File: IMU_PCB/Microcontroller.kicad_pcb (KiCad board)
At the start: 2 copper layers, 103.7 x 64.2 mm, 29 parts, among them J1 Conn_01x02, J4 Conn_01x02_Pin, U1 TPS54560BQDDARQ1, U10 Thermal Resistor, U2 ESP32-DEVKIT-C, U6 TJA1050T/CM,118, U7 Adafruit ICM-20948, U8 SDIO Card Breakout Board, U9 AM2302

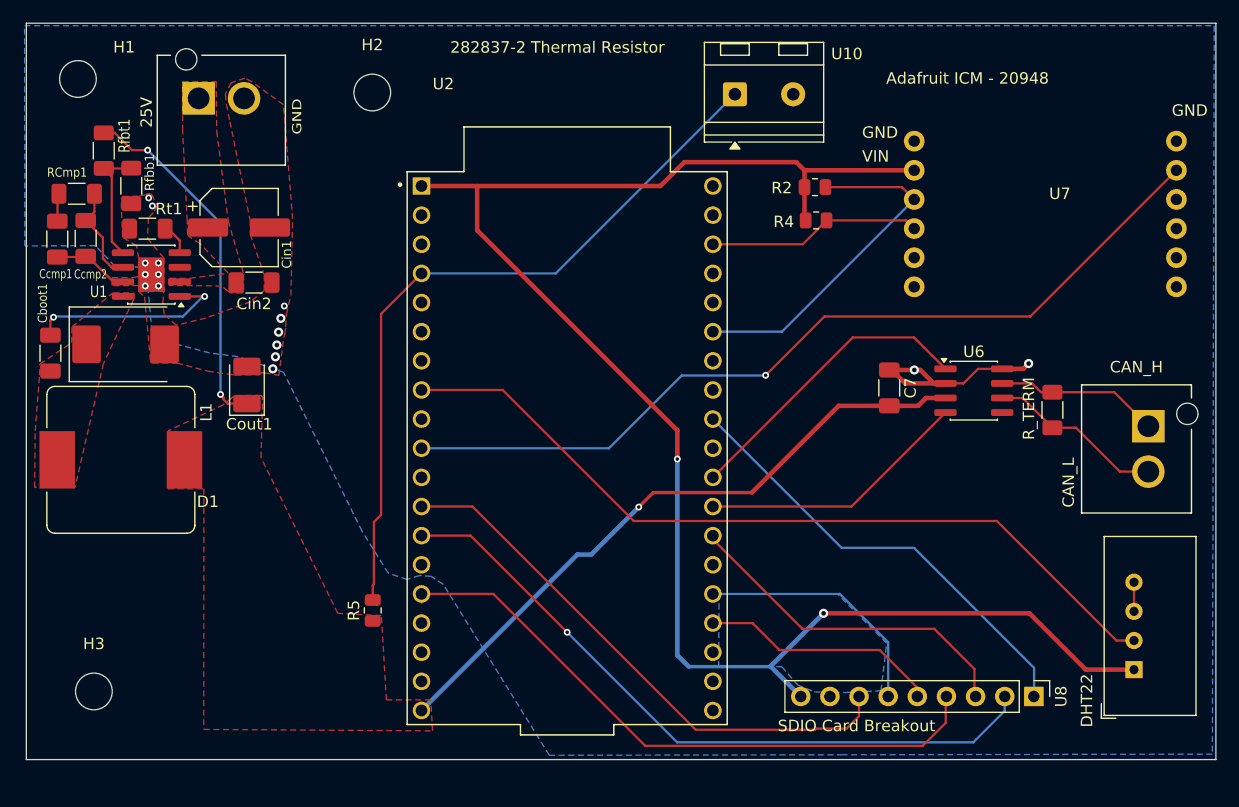
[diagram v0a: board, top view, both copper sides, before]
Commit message: small updates to buck, fixed vias, and remove connection to input connector ground pad
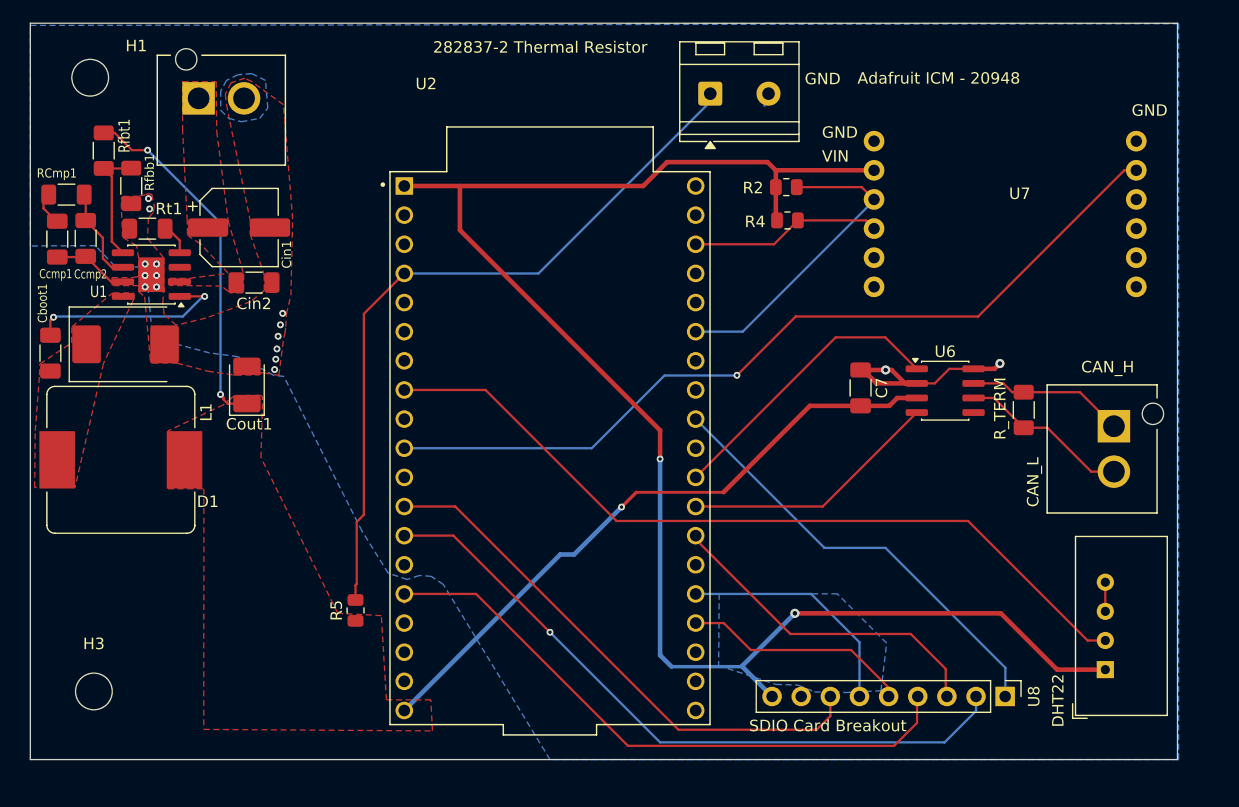
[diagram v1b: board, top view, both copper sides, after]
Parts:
- removed H2: MountingHole, MountingHole:MountingHole_3.2mm_M3
- moved U7 3.50 mm to (186.8, 62.7)
- moved J4 3.00 mm to (193.9, 81.9)
- moved C7 2.50 mm to (172.9, 76.6)
- moved R2 2.50 mm to (166.4, 59.1)
- moved R4 2.50 mm to (166.5, 62.0)
- moved R8 2.50 mm to (187.1, 78.5)
- moved U6 2.50 mm to (180.2, 76.8)
- moved U8 2.50 mm to (185.5, 103.5)
- moved U9 2.50 mm to (194.2, 101.2)
- moved U10 2.15 mm to (159.8, 51.0)
- moved R5 1.50 mm to (128.8, 96.0)
- moved U2 1.50 mm to (145.8, 81.8)
- moved H1 1.08 mm to (105.7, 49.6)
- moved RCmp1 0.89 mm to (103.7, 59.8)
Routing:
- net Net-(U2-3V3): track 149.4 -> 146.4 mm
- net Net-(U2-IO21): track 30.5 -> 27.6 mm
- net Net-(U2-IO22): track 18.7 -> 16.7 mm
- net Net-(U2-IO26): track 75.9 -> 73.9 mm
- net Net-(U2-IO4): track 30.2 -> 29.2 mm
- net Net-(U2-IO33): track 71.2 -> 70.2 mm
- net Net-(U2-IO2): track 21.7 -> 20.7 mm
- net Net-(U2-IO18): track 39.4 -> 38.4 mm
- net Net-(U2-IO17): track 26.5 -> 25.5 mm
- net Net-(U2-IO16): track 23.7 -> 22.7 mm
- net Net-(U2-IO15): track 20.9 -> 19.9 mm
- net Net-(U2-IO13): track 55.1 -> 54.1 mm
- net Net-(U2-IO12): track 61.0 -> 60.0 mm
- net Net-(U2-IO14): track 48.7 -> 47.7 mm
- net /BUCK_5V: track 87.8 -> 86.8 mm
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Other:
- board size 103.7 x 64.2 mm -> 100 x 64.2 mm
- board text removed: "25V"

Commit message: PDB_Schematic mostly updated
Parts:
- removed R2, R4: 10k, Resistor_SMD:R_0805_2012Metric
- added H2: MountingHole, MountingHole:MountingHole_3.2mm_M3, F.Cu at (196.2, 56.2)
- added H4: MountingHole, MountingHole:MountingHole_3.2mm_M3, F.Cu at (195.8, 106.9)
- U10: footprint TerminalBlock_RND:TerminalBlock_RND_205-00232_1x02_P5.08mm_Horizontal -> PROVE-footprints:TE_1877285-2
- U7: value Adafruit ICM-20948 -> SparkFun: ISM330DHCX, MMC5983MA; footprint PROVE-footprints:Adafruit_ICM20948_2x6_Module -> PROVE-footprints:SparkFun 9DoF IMU Breakout - ISM330DHCX, MMC5983MA (Qwiic); moved to B.Cu
- U8: footprint Connector_PinHeader_2.54mm:PinHeader_1x09_P2.54mm_Vertical -> PROVE-footprints:Adafruit SDIO card breakout
- moved U10 47.3 mm to (194.2, 83.4), turned to -90 degrees
- moved R5 44.8 mm to (172.8, 104.8)
- moved U6 29.8 mm to (184.0, 106.4)
- moved C7 29.3 mm to (178.6, 105.3)
- moved U9 28.7 mm to (192.9, 72.5)
- moved R8 26.3 mm to (190.4, 104.6)
- moved U7 15.8 mm to (188.0, 78.4), turned to 90 degrees
- moved J4 14.1 mm to (194.1, 96.0)
- moved Cin1 7.00 mm to (118.7, 69.6)
- moved Cboot1 7.00 mm to (102.2, 80.6)
- moved Cin2 7.00 mm to (120.0, 74.4)
- moved Cout1 7.00 mm to (119.4, 83.3)
- moved D1 7.00 mm to (108.8, 79.8)
- moved J1 7.00 mm to (117.2, 59.4)
- moved L1 7.00 mm to (108.4, 89.9)
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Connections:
- U2 pad 10: Net-(U2-IO26) -> unconnected-(U2-IO26-Pad10)
- U2 pad 31: unconnected-(U2-IO19-Pad31) -> Net-(U2-IO19)
- U2 pad 37: unconnected-(U2-IO23-Pad37) -> Net-(U2-IO23)
- U6 pad 1: Net-(U2-IO17) -> Net-(U2-IO16)
- U6 pad 4: Net-(U2-IO16) -> Net-(U2-IO17)
- U7 pad 1: GND -> Net-(U2-IO19)
- U7 pad 10: unconnected-(U7-Pin_10-Pad10) -> Net-(U2-IO21)
- U7 pad 11: Net-(U2-IO26) -> Net-(U2-3V3)
- U7 pad 2: Net-(U2-3V3) -> unconnected-(U7-Pin_2-Pad2)
- U7 pad 3: Net-(U2-IO21) -> Net-(U2-IO23)
- U7 pad 4: Net-(U2-IO22) -> unconnected-(U7-Pin_4-Pad4)
- U7 pad 9: unconnected-(U7-Pin_9-Pad9) -> Net-(U2-IO22)
- U8 pad 1: Net-(U2-IO18) -> Net-(U2-3V3)
- U8 pad 2: Net-(U2-IO12) -> GND
- U8 pad 3: Net-(U2-IO4) -> Net-(U2-IO14)
- U8 pad 4: Net-(U2-IO13) -> Net-(U2-IO2)
- U8 pad 6: Net-(U2-IO2) -> Net-(U2-IO13)
- U8 pad 7: Net-(U2-IO14) -> Net-(U2-IO4)
- U8 pad 8: GND -> Net-(U2-IO12)
- U8 pad 9: Net-(U2-3V3) -> Net-(U2-IO18)
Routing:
- net Net-(U2-IO26): track 73.9 -> 0.00 mm, vias 1 -> 0
- net Net-(U10-Pin_1): track 64.0 -> 126.8 mm, vias 0 -> 1
- net /BUCK_5V: track 86.8 -> 46.0 mm, vias 3 -> 6
- net Net-(U2-IO23): track 0.00 -> 35.7 mm
- net Net-(U2-3V3): track 146.4 -> 113.7 mm, vias 2 -> 0
- net Net-(U2-IO19): track 0.00 -> 31.2 mm
- net Net-(U2-IO18): track 38.4 -> 7.73 mm
- net Net-(U2-IO14): track 47.7 -> 76.5 mm, vias 0 -> 1
- net Net-(U2-IO16): track 22.7 -> 50.5 mm
- net Net-(U2-IO17): track 25.5 -> 52.5 mm
- net Net-(U2-IO21): track 27.6 -> 8.24 mm
- net Net-(U2-IO13): track 54.1 -> 67.2 mm
- net Net-(U2-IO4): track 29.2 -> 16.6 mm
- net Net-(U2-IO22): track 16.7 -> 6.16 mm
- net Net-(U2-IO15): track 19.9 -> 29.8 mm, vias 0 -> 1
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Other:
- board size 100 x 64.2 mm -> 100 x 59.2 mm
- board text added: "M3"
- board text removed: "282837-2 Thermal Resistor"

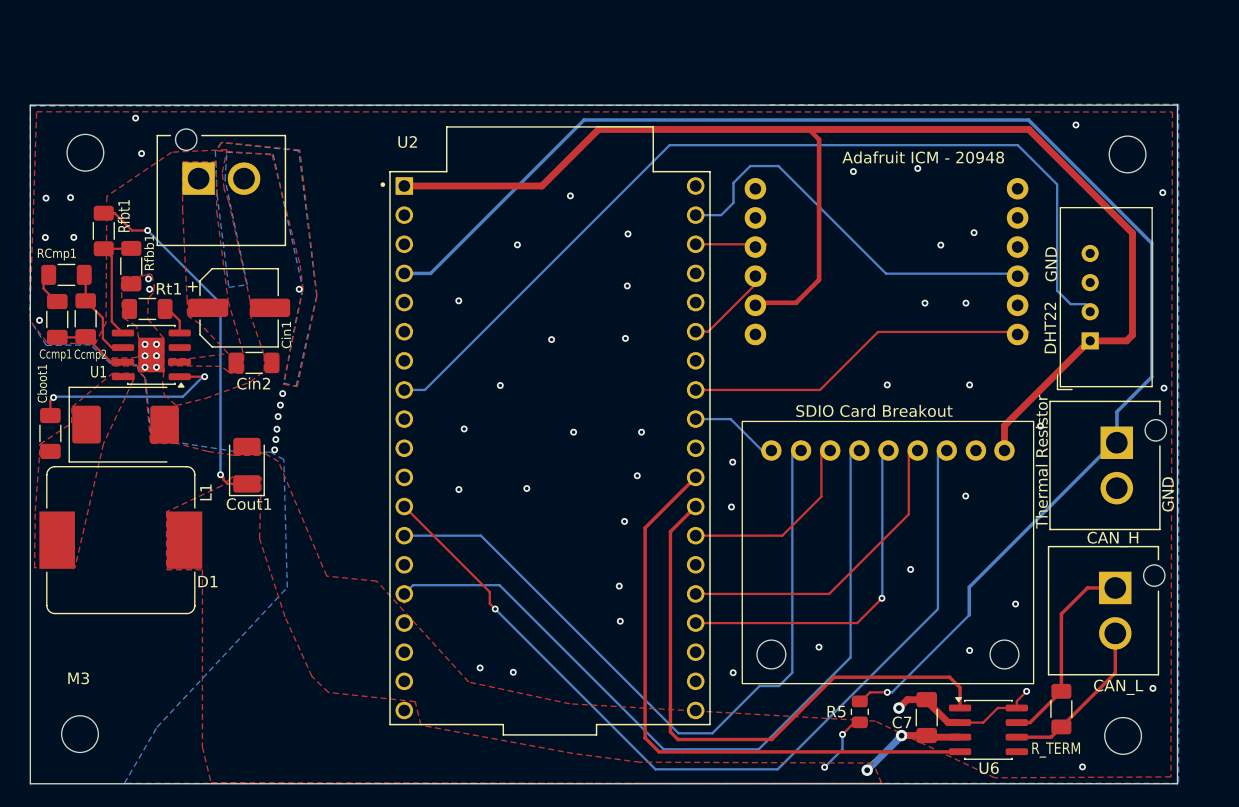
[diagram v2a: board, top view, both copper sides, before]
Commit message: sry forgot to push, waiting on PCB shipping atm. Notes: split power distribution into two boards, one for the main 25V distribution, and another for 12V stuff. Also updated CAN transciever. the previous one was a 5V logic one (same logic as its power), and would have fried our ESPs data pins
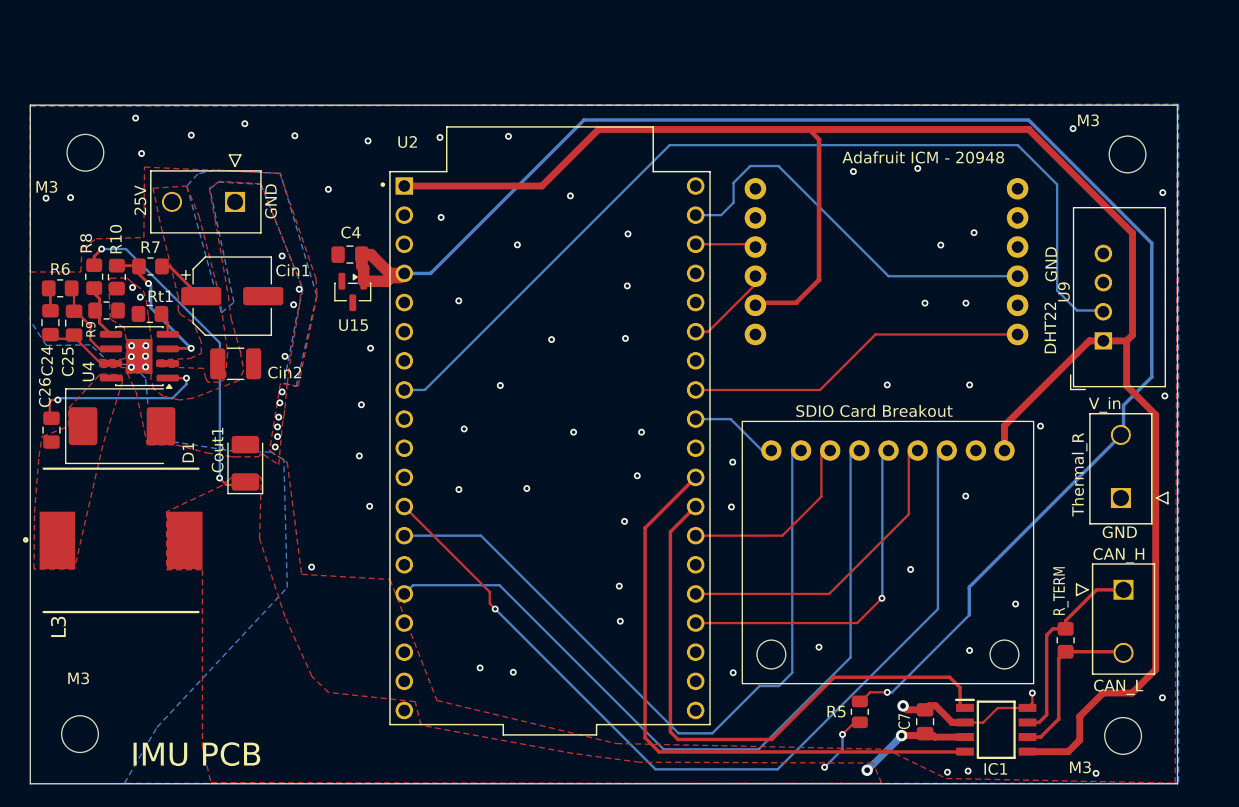
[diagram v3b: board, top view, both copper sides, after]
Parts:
- removed Cboot1: 100nF, Capacitor_SMD:C_1206_3216Metric_Pad1.33x1.80mm_HandSolder
- removed Ccmp1: 10nF, Capacitor_SMD:C_1206_3216Metric_Pad1.33x1.80mm_HandSolder
- removed Ccmp2: 10pF, Capacitor_SMD:C_1206_3216Metric_Pad1.33x1.80mm_HandSolder
- removed J1: Conn_01x02, PROVE-footprints:TE_1877285-2
- removed J4: Conn_01x02_Pin, PROVE-footprints:TE_1877285-2
- removed L1: 22uH, Inductor_SMD:L_Bourns_SRP1245A
- removed RCmp1: 18.2kOhm, Resistor_SMD:R_1206_3216Metric_Pad1.30x1.75mm_HandSolder
- removed Rfbb1: 11.8kOhm, Resistor_SMD:R_1206_3216Metric_Pad1.30x1.75mm_HandSolder
- removed Rfbt1: 64.9kOhm, Resistor_SMD:R_1206_3216Metric_Pad1.30x1.75mm_HandSolder
- removed U1: TPS54560BQDDARQ1, Package_SO:SOIC-8-1EP_3.9x4.9mm_P1.27mm_EP2.29x3mm
- removed U10: Thermal Resistor, PROVE-footprints:TE_1877285-2
- removed U6: TJA1050T/CM,118, Package_SO:SOIC-8_3.9x4.9mm_P1.27mm
- added C24: 10nF, Capacitor_SMD:C_0805_2012Metric_Pad1.18x1.45mm_HandSolder, F.Cu at (102.3, 70.9)
- added C25: 10pF, Capacitor_SMD:C_0805_2012Metric_Pad1.18x1.45mm_HandSolder, F.Cu at (104.3, 71.0)
- added C26: 100nF, Capacitor_SMD:C_0805_2012Metric_Pad1.18x1.45mm_HandSolder, F.Cu at (102.3, 80.3)
- added C4: 10nF, Capacitor_SMD:C_0805_2012Metric_Pad1.18x1.45mm_HandSolder, F.Cu at (128.4, 65.0)
- added IC1: TJA1044BT/0Z, PROVE-footprints:SOIC127P600X175-8N, F.Cu at (184.7, 106.4)
- added J2: 39-28-1023, PROVE-footprints:39-28-1023, F.Cu at (195.8, 94.2)
- added J25: 39-28-1023, PROVE-footprints:39-28-1023, F.Cu at (118.3, 60.4)
- added L3: SRP1265A-220M, PROVE-footprints:SRP1265A, F.Cu at (108.4, 89.9)
- added R10: 38.3k, Resistor_SMD:R_0805_2012Metric_Pad1.20x1.40mm_HandSolder, F.Cu at (108.0, 66.9)
- added R6: 18.2k, Resistor_SMD:R_0805_2012Metric_Pad1.20x1.40mm_HandSolder, F.Cu at (103.1, 67.9)
- added R7: 590k, Resistor_SMD:R_0805_2012Metric_Pad1.20x1.40mm_HandSolder, F.Cu at (111.0, 66.0)
- added R9: 11.8kOhm, Resistor_SMD:R_0805_2012Metric_Pad1.20x1.40mm_HandSolder, F.Cu at (107.1, 69.9)
- added R_TERM1: 120, Resistor_SMD:R_0805_2012Metric_Pad1.20x1.40mm_HandSolder, F.Cu at (190.8, 98.6)
- added Thermal_R1: 39-28-1023, PROVE-footprints:39-28-1023, F.Cu at (195.6, 86.2)
- added U15: LM4040CELT-3.0, Package_TO_SOT_SMD:SOT-23, F.Cu at (128.6, 68.2)
- added U4: TPS54560BQDDARQ1, Package_SO:SOIC-8-1EP_3.9x4.9mm_P1.27mm_EP2.29x3mm, F.Cu at (110.0, 73.8)
- C7: value 0.1u -> 100nF; footprint Capacitor_SMD:C_1206_3216Metric_Pad1.33x1.80mm_HandSolder -> Capacitor_SMD:C_0805_2012Metric_Pad1.18x1.45mm_HandSolder
- Cin2: footprint Capacitor_SMD:C_1206_3216Metric_Pad1.33x1.80mm_HandSolder -> Capacitor_SMD:C_1210_3225Metric_Pad1.33x2.70mm_HandSolder
- R8: value 120 -> 64.9kOhm; footprint Resistor_SMD:R_1206_3216Metric_Pad1.30x1.75mm_HandSolder -> Resistor_SMD:R_0805_2012Metric_Pad1.20x1.40mm_HandSolder
- Rt1: footprint Resistor_SMD:R_1206_3216Metric_Pad1.30x1.75mm_HandSolder -> Resistor_SMD:R_0805_2012Metric_Pad1.20x1.40mm_HandSolder
- U9: footprint Sensor:ASAIR_AM2302_P2.54mm_Vertical -> PROVE-footprints:ASAIR_AM2302_P2.54mm_Vertical
- moved R8 92.4 mm to (106.1, 66.9), turned to 90 degrees
- moved Cin2 1.60 mm to (118.4, 74.5)
- moved Cin1 1.18 mm to (118.1, 68.6)
- moved U9 1.15 mm to (194.0, 72.5)
- moved Rt1 0.49 mm to (110.9, 70.2)
- moved C7 0.39 mm to (178.5, 105.7), turned to 90 degrees
- moved D1 0.34 mm to (108.5, 79.9)
- moved Cout1 0.22 mm to (119.2, 83.2)
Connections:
- net Net-(J1-Pin_1) renamed /buck/25V_IN
- net Net-(U2-3V3) renamed /3v3
- C7 pad 1: GND -> /BUCK_5V
- C7 pad 2: /BUCK_5V -> GND
- R8 pad 2: Net-(J4-Pin_2) -> /BUCK_5V
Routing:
- net /3v3: track 113.7 -> 158.7 mm
- net Net-(U1-BOOT): track 17.8 -> 0.00 mm, vias 2 -> 0
- net /CANH: track 0.00 -> 17.6 mm
- net Net-(U4-BOOT): track 0.00 -> 15.9 mm, vias 0 -> 2
- net /CANL: track 0.00 -> 14.6 mm
- net Net-(J4-Pin_2): track 14.4 -> 0.00 mm
- net Net-(U4-EN): track 0.00 -> 13.0 mm, vias 0 -> 2
- net Net-(U4-FB): track 17.4 -> 4.66 mm
- net Net-(U15-K): track 126.8 -> 137.4 mm
- net Net-(U1-FB): track 10.5 -> 0.00 mm
- net Net-(U1-COMP): track 8.74 -> 0.00 mm
- net Net-(U4-COMP): track 0.00 -> 7.24 mm
- net /buck/25V_IN: track 0.00 -> 4.50 mm
- net Net-(Ccmp1-Pad2): track 3.05 -> 0.00 mm
- net Net-(C24-Pad2): track 0.00 -> 1.92 mm
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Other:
- board text added: "25V"
- board text added: "IMU PCB"
- board text added: "Thermal_R"
- board text added: "V_in"
